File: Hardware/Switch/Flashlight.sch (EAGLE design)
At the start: 11 parts

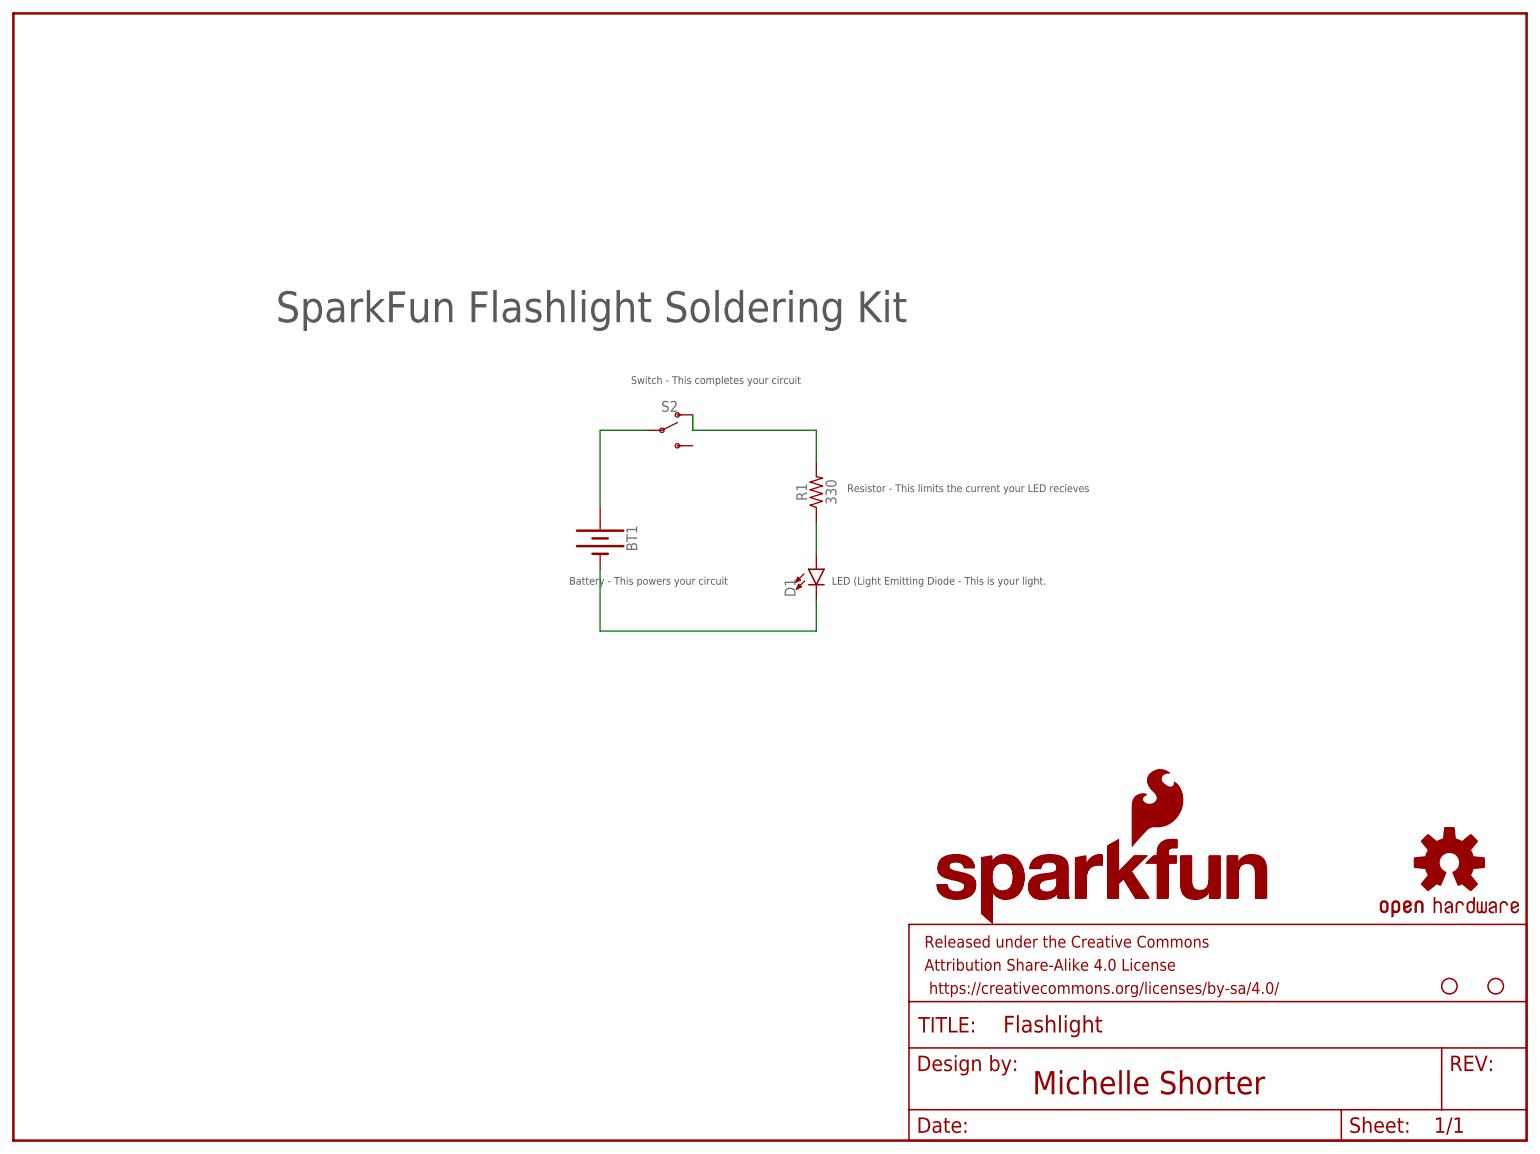
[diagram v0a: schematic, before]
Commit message: Protos
This is what was sent out for protos.
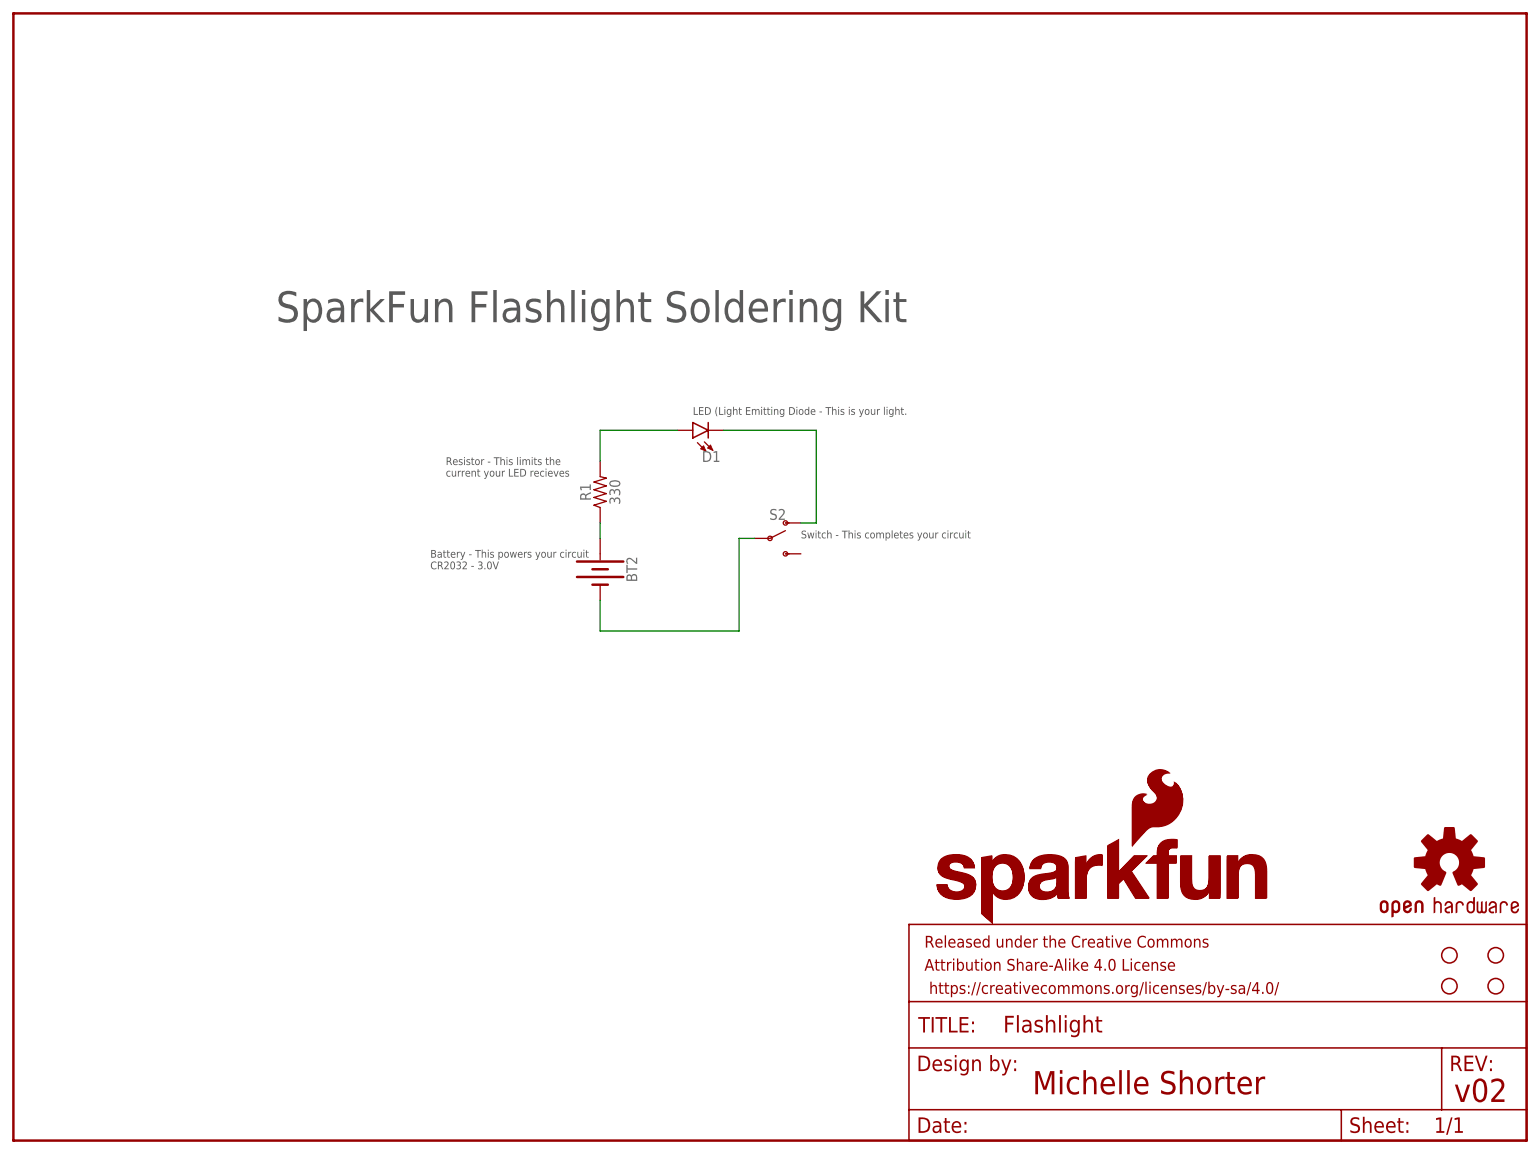
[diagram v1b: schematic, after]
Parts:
- removed BT1: (no value), SparkFun-Batteries:BATTERY-20MM_SMD
- added BT2: (no value), SparkFun-Batteries:BATTERY-20MM_PTH_KIT
- added H3, H4: STAND-OFF, SparkFun-Hardware:STAND-OFF
- D1: device SparkFun-LED:LED5MM-KIT -> SparkFun-LED:LED-5MM-KIT-NO-SILK; PROD_ID (none) -> 9903
- R1: PROD_ID (none) -> 8371
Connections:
- removed net BATT: BT1.+, S2.P
- removed net N$2: R1.2, S2.O
- removed net N$3: D1.A, R1.1
- new net ANODE: D1.A, R1.2
- new net CATHODE: D1.C, S2.O
- new net VBATT: BT2.+, R1.1
- net GND: now also BT2.-, S2.P; no longer BT1.-, D1.C
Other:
- note added: "Battery - This powers your circuit CR2032 - 3.0V"
- note added: "v02"
- note removed: "Battery - This powers your circuit"
- moved on the sheet: D1, R1, S2
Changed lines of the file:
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@@
 <layer number="19" name="Unrouted" color="6" fill="1" visible="no" active="no"/>
 <layer number="20" name="Dimension" color="15" fill="1" visible="no" active="no"/>
-<layer number="21" name="tPlace" color="7" fill="1" visible="no" active="no"/>
-<layer number="22" name="bPlace" color="7" fill="1" visible="no" active="no"/>
+<layer number="21" name="tPlace" color="16" fill="1" visible="no" active="no"/>
+<layer number="22" name="bPlace" color="14" fill="1" visible="no" active="no"/>
 <layer number="23" name="tOrigins" color="15" fill="1" visible="no" active="no"/>
 <layer number="24" name="bOrigins" color="15" fill="1" visible="no" active="no"/>
@@
 <layer number="49" name="Reference" color="7" fill="1" visible="no" active="no"/>
 <layer number="50" name="dxf" color="7" fill="1" visible="no" active="no"/>
-<layer number="51" name="tDocu" color="7" fill="1" visible="no" active="no"/>
+<layer number="51" name="tDocu" color="6" fill="1" visible="no" active="no"/>
 <layer number="52" name="bDocu" color="7" fill="1" visible="no" active="no"/>
 <layer number="53" name="tGND_GNDA" color="7" fill="9" visible="no" active="no"/>
@@
 <layer number="59" name="tCarbon" color="7" fill="1" visible="no" active="no"/>
 <layer number="60" name="bCarbon" color="7" fill="1" visible="no" active="no"/>
+<layer number="88" name="SimResults" color="9" fill="1" visible="yes" active="yes"/>
+<layer number="89" name="SimProbes" color="9" fill="1" visible="yes" active="yes"/>
 <layer number="90" name="Modules" color="5" fill="1" visible="yes" active="yes"/>
 <layer number="91" name="Nets" color="2" fill="1" visible="yes" active="yes"/>
@@
 </classes>
 <parts>
-<part name="BT1" library="SparkFun-Batteries" deviceset="BATTERY" device="-20MM_SMD"/>
 <part name="FRAME1" library="SparkFun-Aesthetics" deviceset="FRAME-LETTER" device=""/>
 <part name="LOGO1" library="SparkFun-Aesthetics" deviceset="OSHW-LOGO" device="S"/>
-<part name="D1" library="SparkFun-LED" deviceset="LED" device="5MM-KIT"/>
-<part name="R1" library="SparkFun-Resistors" deviceset="RESISTOR" device="AXIAL-0.3-KIT" value="330"/>
+<part name="D1" library="SparkFun-LED" deviceset="LED" device="-5MM-KIT-NO-SILK">
+<attribute name="PROD_ID" value="9903"/>
+</part>
+<part name="R1" library="SparkFun-Resistors" deviceset="RESISTOR" device="AXIAL-0.3-KIT" value="330">
+<attribute name="PROD_ID" value="8371"/>
+</part>
 <part name="LOGO2" library="SparkFun-Aesthetics" deviceset="SFE_LOGO_FLAME" device=".1_INCH"/>
 <part name="H1" library="SparkFun-Hardware" deviceset="STAND-OFF" device=""/>
@@
 <part name="LOGO4" library="SparkFun-Aesthetics" deviceset="SFE_LOGO_NAME" device=".1_INCH"/>
 <part name="LOGO3" library="SparkFun-Aesthetics" deviceset="SFE_LOGO_NAME_FLAME" device=".2_INCH"/>
+<part name="BT2" library="SparkFun-Batteries" deviceset="BATTERY" device="-20MM_PTH_KIT">
+<attribute name="PROD_ID" value="9031"/>
+</part>
+<part name="H3" library="SparkFun-Hardware" deviceset="STAND-OFF" device=""/>
+<part name="H4" library="SparkFun-Hardware" deviceset="STAND-OFF" device=""/>
 </parts>
 <sheets>
@@
 <text x="167.64" y="7.62" size="3.81" layer="94">Michelle Shorter</text>
 <text x="43.18" y="134.62" size="5.08" layer="97" font="vector">SparkFun Flashlight Soldering Kit</text>
-<text x="134.62" y="91.44" size="1.27" layer="97">LED (Light Emitting Diode - This is your light.</text>
-<text x="137.16" y="106.68" size="1.27" layer="97">Resistor - This limits the current your LED recieves</text>
-<text x="101.6" y="124.46" size="1.27" layer="97">Switch - This completes your circuit</text>
-<text x="91.44" y="91.44" size="1.27" layer="97">Battery - This powers your circuit</text>
+<text x="111.76" y="119.38" size="1.27" layer="97">LED (Light Emitting Diode - This is your light.</text>
+<text x="71.12" y="109.22" size="1.27" layer="97">Resistor - This limits the
+current your LED recieves</text>
+<text x="129.54" y="99.06" size="1.27" layer="97">Switch - This completes your circuit</text>
+<text x="68.58" y="93.98" size="1.27" layer="97">Battery - This powers your circuit
+CR2032 - 3.0V</text>
+<text x="236.982" y="6.35" size="3.81" layer="94">v02</text>
 </plain>
 <instances>
-<instance part="BT1" gate="G$1" x="96.52" y="99.06" rot="R270"/>
 <instance part="FRAME1" gate="G$1" x="0" y="0"/>
 <instance part="FRAME1" gate="V" x="147.32" y="0"/>
 <instance part="LOGO1" gate="G$1" x="236.22" y="45.72"/>
-<instance part="D1" gate="G$1" x="132.08" y="93.98"/>
-<instance part="R1" gate="G$1" x="132.08" y="106.68" rot="R90"/>
+<instance part="D1" gate="G$1" x="111.76" y="116.84" rot="R90">
+<attribute name="PROD_ID" x="111.76" y="116.84" size="1.778" layer="96" rot="R90" display="off"/>
+</instance>
+<instance part="R1" gate="G$1" x="96.52" y="106.68" rot="R90"/>
 <instance part="LOGO2" gate="G$1" x="183.642" y="47.752"/>
 <instance part="H1" gate="G$1" x="236.22" y="25.4"/>
 <instance part="H2" gate="G$1" x="243.84" y="25.4"/>
-<instance part="S2" gate="1" x="106.68" y="116.84"/>
+<instance part="S2" gate="1" x="124.46" y="99.06"/>
 <instance part="LOGO4" gate="G$1" x="149.86" y="35.56"/>
 <instance part="LOGO3" gate="G$1" x="151.13" y="35.306"/>
+<instance part="BT2" gate="G$1" x="96.52" y="93.98" rot="R270">
+<attribute name="PROD_ID" x="96.52" y="93.98" size="1.778" layer="96" rot="R270" display="off"/>
+</instance>
+<instance part="H3" gate="G$1" x="236.22" y="30.48"/>
+<instance part="H4" gate="G$1" x="243.84" y="30.48"/>
 </instances>
 <busses>
 </busses>
 <nets>
-<net name="BATT" class="0">
-<segment>
-<wire x1="96.52" y1="116.84" x2="104.14" y2="116.84" width="0.1524" layer="91"/>
-<pinref part="BT1" gate="G$1" pin="+"/>
-<wire x1="96.52" y1="116.84" x2="96.52" y2="104.14" width="0.1524" layer="91"/>
+<net name="GND" class="0">
+<segment>
 <pinref part="S2" gate="1" pin="P"/>
-</segment>
-</net>
-<net name="N$2" class="0">
-<segment>
-<wire x1="111.76" y1="116.84" x2="132.08" y2="116.84" width="0.1524" layer="91"/>
+<wire x1="121.92" y1="99.06" x2="119.38" y2="99.06" width="0.1524" layer="91"/>
+<wire x1="119.38" y1="99.06" x2="119.38" y2="83.82" width="0.1524" layer="91"/>
+<pinref part="BT2" gate="G$1" pin="-"/>
+<wire x1="96.52" y1="88.9" x2="96.52" y2="83.82" width="0.1524" layer="91"/>
+<wire x1="119.38" y1="83.82" x2="96.52" y2="83.82" width="0.1524" layer="91"/>
+</segment>
+</net>
+<net name="ANODE" class="0">
+<segment>
 <pinref part="R1" gate="G$1" pin="2"/>
-<wire x1="132.08" y1="116.84" x2="132.08" y2="111.76" width="0.1524" layer="91"/>
+<pinref part="D1" gate="G$1" pin="A"/>
+<wire x1="96.52" y1="111.76" x2="96.52" y2="116.84" width="0.1524" layer="91"/>
+<wire x1="96.52" y1="116.84" x2="109.22" y2="116.84" width="0.1524" layer="91"/>
+</segment>
+</net>
+<net name="CATHODE" class="0">
+<segment>
+<pinref part="D1" gate="G$1" pin="C"/>
 <pinref part="S2" gate="1" pin="O"/>
-<wire x1="111.76" y1="119.38" x2="111.76" y2="116.84" width="0.1524" layer="91"/>
-</segment>
-</net>
-<net name="N$3" class="0">
-<segment>
+<wire x1="116.84" y1="116.84" x2="132.08" y2="116.84" width="0.1524" layer="91"/>
+<wire x1="132.08" y1="116.84" x2="132.08" y2="101.6" width="0.1524" layer="91"/>
+<wire x1="132.08" y1="101.6" x2="129.54" y2="101.6" width="0.1524" layer="91"/>
+</segment>
+</net>
+<net name="VBATT" class="0">
+<segment>
+<pinref part="BT2" gate="G$1" pin="+"/>
 <pinref part="R1" gate="G$1" pin="1"/>
-<pinref part="D1" gate="G$1" pin="A"/>
-<wire x1="132.08" y1="101.6" x2="132.08" y2="96.52" width="0.1524" layer="91"/>
-</segment>
-</net>
-<net name="GND" class="0">
-<segment>
-<pinref part="D1" gate="G$1" pin="C"/>
-<wire x1="132.08" y1="88.9" x2="132.08" y2="83.82" width="0.1524" layer="91"/>
-<wire x1="132.08" y1="83.82" x2="96.52" y2="83.82" width="0.1524" layer="91"/>
-<pinref part="BT1" gate="G$1" pin="-"/>
-<wire x1="96.52" y1="93.98" x2="96.52" y2="83.82" width="0.1524" layer="91"/>
+<wire x1="96.52" y1="99.06" x2="96.52" y2="101.6" width="0.1524" layer="91"/>
 </segment>
 </net>
@@
 </schematic>
 </drawing>
+<compatibility>
+<note version="6.3" minversion="6.2.2" severity="warning">
+Since Version 6.2.2 text objects can contain more than one line,
+which will not be processed correctly with this version.
+</note>
+</compatibility>
 </eagle>
